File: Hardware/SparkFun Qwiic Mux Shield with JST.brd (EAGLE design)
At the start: 53.3 x 59.7 mm, 35 parts, among them Q1 200mA/50V, Q2 200mA/50V, U1 ARDUINO UNO

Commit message: Adding Mux Shield
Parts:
- removed J21, J22: (no value), SparkX:1X18_NO_SILK
- removed Q1, Q2: 200mA/50V, SparkFun-DiscreteSemi:SOT23-3
- added C1: 0.1uF, SparkFun-Capacitors:0603
- added C2, C3, C4, C5: 1.0uF, SparkFun-Capacitors:0603
- added J23, J24, J25, J26: (no value), SparkX:1X04
- added J29, J30: (no value), SparkFun-Connectors:1X08_NO_SILK
- added JP1, JP2, JP3: (no value), SparkFun-Jumpers:SMT-JUMPER_2_NO_SILK
- added R1, R10, R11, R12, R13, R14, R15, R16, R17, R18, R6, R7, R8, R9: 4.7K, SparkFun-Resistors:0603-RES
- added R19, R20, R21: 10k, SparkFun-Resistors:0603
- added U2: TCA9548A, SparkX:TSSOP28
- J11, J12, J13, J14, J15, J16, J17, J18, J19, J20, J5, J7: device SparkX:1X18_NO_SILK -> SparkFun-Connectors:1X08_NO_SILK
- moved U$1 42.0 mm to (48.3, 6.35)
- moved R4 30.6 mm to (20.3, 17.8)
- moved R5 27.1 mm to (20.3, 20.3)
- moved R3 22.5 mm to (35.6, 25.4), turned to 270 degrees
- moved R2 17.7 mm to (40.6, 25.4), turned to 270 degrees
- moved J11 17.0 mm to (20.3, 39.4), turned to 90 degrees
- moved J17 16.1 mm to (35.6, 39.4), turned to 90 degrees
- moved J19 16.1 mm to (40.6, 39.4), turned to 90 degrees
- moved J5 15.5 mm to (15.2, 39.4), turned to 90 degrees
- moved J13 15.5 mm to (25.4, 39.4), turned to 90 degrees
- moved J15 15.5 mm to (30.5, 39.4), turned to 90 degrees
- moved J12 13.0 mm to (22.9, 57.1)
- moved J16 8.03 mm to (33.0, 57.1)
- moved J14 8.03 mm to (27.9, 57.1)
- moved J18 5.68 mm to (38.1, 57.1)
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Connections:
- removed net HV_SCL: J4.1, Q2.3, R5.2, U1.A5
- removed net HV_SDA: J4.2, Q1.3, R4.2, U1.A4
- removed net N$100: J19.11, J20.11
- removed net N$101: J19.12, J20.12
- removed net N$102: J19.13, J20.13
- removed net N$103: J19.14, J20.14
- removed net N$104: J19.15, J20.15
- removed net N$105: J19.16, J20.16
- removed net N$106: J19.17, J20.17
- removed net N$107: J19.18, J20.18
- removed net N$108: J19.1, J20.1
- removed net N$109: J21.2, J22.2
- removed net N$110: J21.3, J22.3
- removed net N$111: J21.4, J22.4
- removed net N$112: J21.5, J22.5
- removed net N$113: J21.6, J22.6
- removed net N$114: J21.7, J22.7
- removed net N$115: J21.8, J22.8
- removed net N$116: J21.9, J22.9
- removed net N$117: J21.10, J22.10
- removed net N$118: J21.11, J22.11
- removed net N$119: J21.12, J22.12
- removed net N$120: J21.13, J22.13
- removed net N$121: J21.14, J22.14
- removed net N$122: J21.15, J22.15
- removed net N$123: J21.16, J22.16
- removed net N$124: J21.17, J22.17
- removed net N$125: J21.18, J22.18
- removed net N$126: J21.1, J22.1
- removed net N$49: J13.14, J14.14
- removed net N$50: J13.15, J14.15
- removed net N$51: J13.16, J14.16
- removed net N$52: J13.17, J14.17
- removed net N$53: J13.18, J14.18
- removed net N$54: J13.1, J14.1
- removed net N$55: J15.2, J16.2
- removed net N$56: J15.3, J16.3
- removed net N$65: J15.12, J16.12
- removed net N$66: J15.13, J16.13
- removed net N$67: J15.14, J16.14
- removed net N$68: J15.15, J16.15
- removed net N$69: J15.16, J16.16
- removed net N$70: J15.17, J16.17
- removed net N$71: J15.18, J16.18
- removed net N$72: J15.1, J16.1
- removed net N$73: J17.2, J18.2
- removed net N$74: J17.3, J18.3
- removed net N$75: J17.4, J18.4
- removed net N$76: J17.5, J18.5
- removed net N$77: J17.6, J18.6
- removed net N$78: J17.7, J18.7
- removed net N$79: J17.8, J18.8
- removed net N$80: J17.9, J18.9
- removed net N$81: J17.10, J18.10
- removed net N$82: J17.11, J18.11
- removed net N$83: J17.12, J18.12
- removed net N$84: J17.13, J18.13
- removed net N$85: J17.14, J18.14
- removed net N$86: J17.15, J18.15
- removed net N$87: J17.16, J18.16
- removed net N$88: J17.17, J18.17
- removed net N$89: J17.18, J18.18
- removed net N$90: J17.1, J18.1
- removed net N$91: J19.2, J20.2
- removed net N$92: J19.3, J20.3
- removed net N$93: J19.4, J20.4
- removed net N$94: J19.5, J20.5
- removed net N$95: J19.6, J20.6
- removed net N$96: J19.7, J20.7
- removed net N$97: J19.8, J20.8
- removed net N$98: J19.9, J20.9
- removed net N$99: J19.10, J20.10
- removed net SCL: J1.4, J10.4, J8.4, J9.4, Q2.2, R2.2
- removed net SDA: J1.3, J10.3, J8.3, J9.3, Q1.2, R3.2
- new net ADR0: JP3.1, R19.2, U2.1
- new net ADR1: JP2.1, R20.2, U2.2
- new net ADR2: JP1.1, R21.2, U2.21
- new net MAIN_SCL: J4.1, R5.2, U1.A5, U2.22
- new net MAIN_SCL_1: J3.10, U1.SCL
- new net MAIN_SDA: J4.2, R4.2, U1.A4, U2.23
- new net MAIN_SDA_1: J3.9, U1.SDA
- new net SCL0: J1.4, R7.2, U2.5
- new net SCL2: J9.4, R10.2, U2.9
- new net SCL3: J10.4, R12.2, U2.11
- new net SCL4: J23.4, R3.2, U2.14
- new net SCL5: J24.4, R14.2, U2.16
- new net SCL6: J25.4, R16.2, U2.18
- new net SCL7: J26.4, R18.2, U2.20
- new net SDA0: J1.3, R6.2, U2.4
- new net SDA2: J9.3, R9.2, U2.8
- new net SDA3: J10.3, R11.2, U2.10
- new net SDA4: J23.3, R2.2, U2.13
- new net SDA5: J24.3, R13.2, U2.15
- new net SDA6: J25.3, R15.2, U2.17
- new net SDA7: J26.3, R17.2, U2.19
- net 3.3V: now also C1.1, C2.1, C3.1, C4.1, C5.1, J23.2, J24.2, J25.2, J26.2, JP1.2, JP2.2, JP3.2, R1.1, R10.1, R11.1, R12.1, R13.1, R14.1, R15.1, R16.1, R17.1, R18.1, R6.1, R7.1, R8.1, R9.1, U2.24, U2.3; no longer Q1.1, Q2.1
- net GND: now also C1.2, C2.2, C3.2, C4.2, C5.2, J23.1, J24.1, J25.1, J26.1, R19.1, R20.1, R21.1, U2.12
- net N$1: now also J5.8, J7.1; no longer J5.2, J7.2
- net N$10: now also J11.7, J12.2; no longer J5.11, J7.11
- net N$11: now also J11.6, J12.3; no longer J5.12, J7.12
- net N$12: now also J11.5, J12.4; no longer J5.13, J7.13
- net N$13: now also J11.4, J12.5; no longer J5.14, J7.14
- net N$14: now also J11.3, J12.6; no longer J5.15, J7.15
- net N$15: now also J11.2, J12.7; no longer J5.16, J7.16
- net N$16: now also J11.1, J12.8; no longer J5.17, J7.17
- net N$17: now also J13.8, J14.1; no longer J5.18, J7.18
- net N$18: now also J13.7, J14.2; no longer J5.1, J7.1
- net N$19: now also J13.6, J14.3; no longer J13.2, J14.2
- net N$2: now also J5.7, J7.2; no longer J5.3, J7.3
- net N$20: now also J13.5, J14.4; no longer J13.3, J14.3
- net N$21: now also J13.4, J14.5; no longer J11.2, J12.2
- net N$22: now also J13.3, J14.6; no longer J11.3, J12.3
- net N$23: now also J13.2, J14.7; no longer J11.4, J12.4
- net N$24: now also J13.1, J14.8; no longer J11.5, J12.5
- net N$25: now also J15.8, J16.1; no longer J11.6, J12.6
- net N$26: now also J15.7, J16.2; no longer J11.7, J12.7
- net N$27: now also J15.6, J16.3; no longer J11.8, J12.8
- net N$28: now also J15.5, J16.4; no longer J11.9, J12.9
- net N$29: now also J15.4, J16.5; no longer J11.10, J12.10
- net N$3: now also J5.6, J7.3; no longer J5.4, J7.4
- net N$30: now also J15.3, J16.6; no longer J11.11, J12.11
- net N$31: now also J15.2, J16.7; no longer J11.12, J12.12
- net N$32: now also J15.1, J16.8; no longer J11.13, J12.13
- net N$33: now also J17.8, J18.1; no longer J11.14, J12.14
- net N$34: now also J17.7, J18.2; no longer J11.15, J12.15
- net N$35: now also J17.6, J18.3; no longer J11.16, J12.16
- net N$36: now also J17.5, J18.4; no longer J11.17, J12.17
- net N$37: now also J17.4, J18.5; no longer J11.18, J12.18
- net N$38: now also J17.3, J18.6; no longer J11.1, J12.1
- net N$39: now also J17.2, J18.7; no longer J13.4, J14.4
- net N$4: now also J7.4; no longer J7.5
- net N$40: now also J17.1, J18.8; no longer J13.5, J14.5
- net N$41: now also J19.8, J20.1; no longer J13.6, J14.6
- net N$42: now also J19.7, J20.2; no longer J13.7, J14.7
- net N$43: now also J19.6, J20.3; no longer J13.8, J14.8
- net N$44: now also J19.5, J20.4; no longer J13.9, J14.9
- net N$45: now also J19.4, J20.5; no longer J13.10, J14.10
- net N$46: now also J19.3, J20.6; no longer J13.11, J14.11
- net N$47: now also J19.2, J20.7; no longer J13.12, J14.12
- net N$48: now also J19.1, J20.8; no longer J13.13, J14.13
- net N$5: now also J5.4, J7.5; no longer J5.6, J7.6
- net N$57: now also J29.8, J30.1; no longer J15.4, J16.4
- net N$58: now also J29.7, J30.2; no longer J15.5, J16.5
- net N$59: now also J29.6, J30.3; no longer J15.6, J16.6
- net N$6: now also J5.3, J7.6; no longer J5.7, J7.7
- net N$60: now also J29.5, J30.4; no longer J15.7, J16.7
- net N$61: now also J29.4, J30.5; no longer J15.8, J16.8
- net N$62: now also J29.3, J30.6; no longer J15.9, J16.9
- net N$63: now also J29.2, J30.7; no longer J15.10, J16.10
- net N$64: now also J29.1, J30.8; no longer J15.11, J16.11
- net N$7: now also J5.2, J7.7; no longer J5.8, J7.8
- net N$8: now also J5.1, J7.8; no longer J5.9, J7.9
- net N$9: now also J11.8, J12.1; no longer J5.10, J7.10
- net SCL1: now also J8.4, R8.2, U2.7; no longer J3.10, U1.SCL
- net SDA1: now also J8.3, R1.2, U2.6; no longer J3.9, U1.SDA
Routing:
- net 3.3V: track 79.8 -> 200.0 mm
- net MAIN_SDA: track 0.00 -> 69.4 mm, vias 0 -> 1
- net MAIN_SCL: track 0.00 -> 66.9 mm, vias 0 -> 1
- net HV_SCL: track 53.4 -> 0.00 mm, vias 1 -> 0
- net SDA: track 50.0 -> 0.00 mm
- net HV_SDA: track 47.6 -> 0.00 mm
- net SCL: track 45.2 -> 0.00 mm, vias 5 -> 0
- net 5V: track 26.9 -> 52.8 mm, vias 0 -> 1
- net SDA4: track 0.00 -> 20.8 mm
- net SCL0: track 0.00 -> 20.0 mm
- net ADR1: track 0.00 -> 19.1 mm, vias 0 -> 2
- net SCL7: track 0.00 -> 18.7 mm
- net SDA7: track 0.00 -> 18.6 mm
- net SDA0: track 0.00 -> 18.4 mm
- net SDA3: track 0.00 -> 18.0 mm
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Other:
- board text added: "0"
- board text added: "1"
- board text added: "3.3V"
- board text added: "ADR"
- board text added: "Port"
- board text added: "Qwiic Mux Shield"
- board text added: "SCLx"
- board text added: "SDAx"
- board text removed: "I2C Shield"

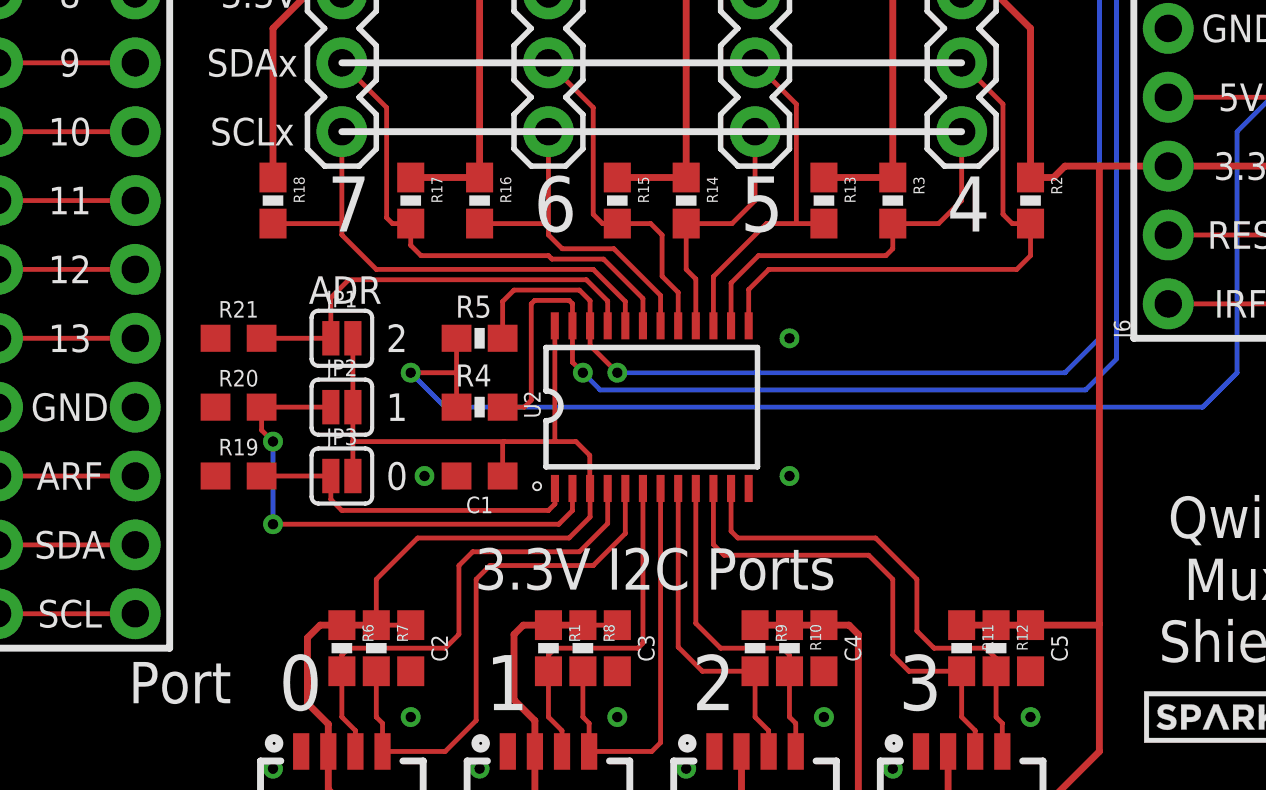
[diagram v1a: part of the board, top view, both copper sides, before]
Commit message: Breaking out reset pin
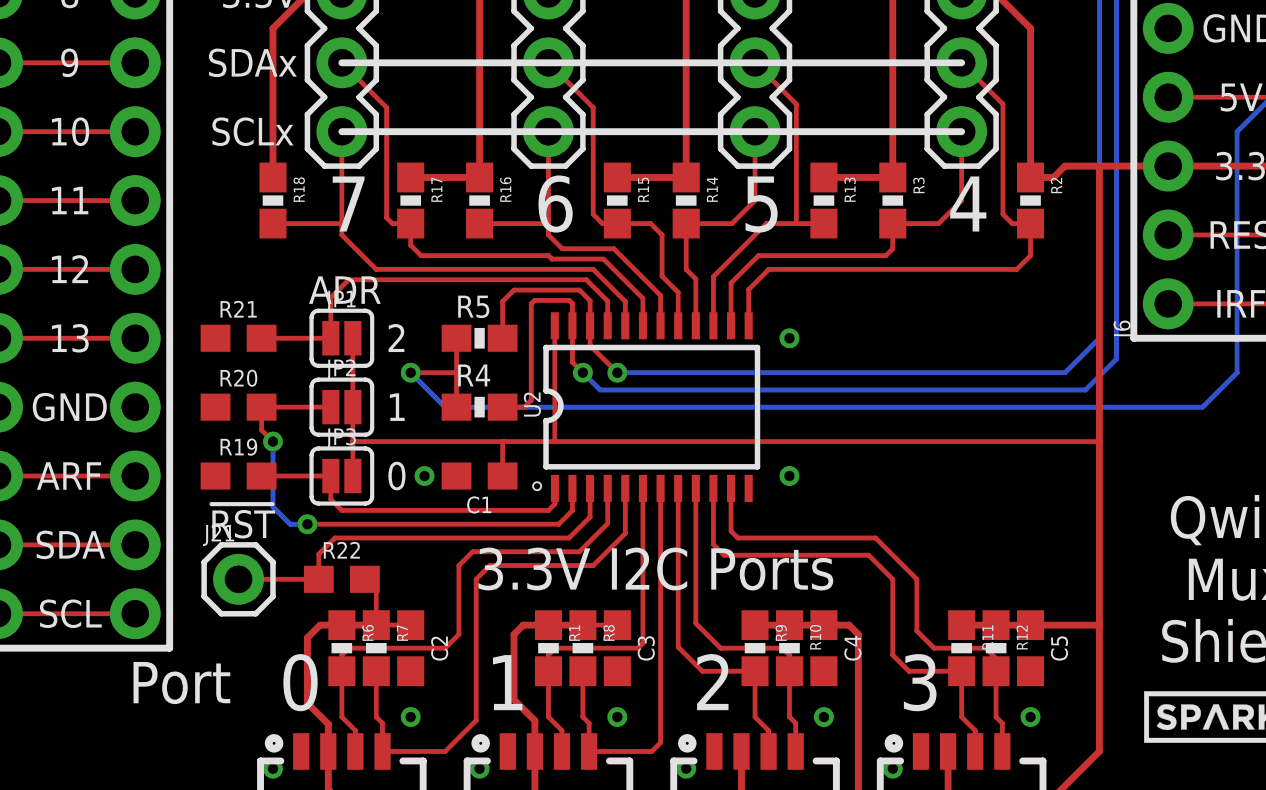
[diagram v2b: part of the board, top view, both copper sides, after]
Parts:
- added J21: (no value), SparkFun-Connectors:1X01
- added R22: 10k, SparkFun-Resistors:0603
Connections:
- new net !RST: J21.1, R22.1, U2.3
- net 3.3V: now also R22.2; no longer U2.3
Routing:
- net !RST: track 0.00 -> 15.5 mm
- net 3.3V: track 200.0 -> 207.4 mm
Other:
- board text added: "!RST"
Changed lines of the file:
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@@
 <layer number="47" name="Measures" color="7" fill="1" visible="no" active="yes"/>
 <layer number="48" name="Document" color="7" fill="1" visible="no" active="yes"/>
-<layer number="49" name="Reference" color="7" fill="1" visible="yes" active="yes"/>
+<layer number="49" name="Reference" color="7" fill="1" visible="no" active="yes"/>
 <layer number="50" name="dxf" color="7" fill="1" visible="no" active="yes"/>
 <layer number="51" name="tDocu" color="6" fill="1" visible="yes" active="yes"/>
@@
 <text x="22.733" y="25.273" size="2.032" layer="22" font="vector" ratio="15" rot="MR0" align="center">6</text>
 <text x="15.113" y="25.273" size="2.032" layer="22" font="vector" ratio="15" rot="MR0" align="center">7</text>
+<text x="11.557" y="13.462" size="1.016" layer="21" font="vector" ratio="15" align="center">!RST</text>
 </plain>
 <attributes>
@@
 <attribute name="PROD_ID" value="CONN-08438" x="43.18" y="57.15" size="1.778" layer="27" rot="R270" display="off"/>
 </element>
+<element name="R22" library="SparkFun-Resistors" package="0603" value="10k" x="15.24" y="11.43">
+<attribute name="PROD_ID" value="RES-00824" x="15.24" y="11.43" size="1.778" layer="27" font="vector" ratio="15" display="off"/>
+</element>
+<element name="J21" library="SparkFun-Connectors" package="1X01" value="" x="11.43" y="11.43"/>
 </elements>
 <signals>
@@
 <contactref element="J10" pad="2"/>
 <contactref element="U2" pad="24"/>
-<contactref element="U2" pad="3"/>
 <contactref element="R6" pad="1"/>
 <contactref element="R7" pad="1"/>
@@
 <wire x1="15.6464" y1="17.78" x2="15.6464" y2="20.32" width="0.1778" layer="1"/>
 <wire x1="21.17" y1="15.24" x2="21.17" y2="16.471" width="0.1778" layer="1"/>
-<wire x1="23.876" y1="16.51" x2="23.114" y2="16.51" width="0.1778" layer="1"/>
-<wire x1="23.114" y1="16.51" x2="21.209" y2="16.51" width="0.1778" layer="1"/>
 <wire x1="21.209" y1="16.51" x2="15.6464" y2="16.51" width="0.1778" layer="1"/>
-<wire x1="23.876" y1="16.51" x2="24.384" y2="16.002" width="0.1778" layer="1"/>
-<wire x1="24.384" y1="16.002" x2="24.384" y2="14.791" width="0.1778" layer="1"/>
-<wire x1="24.384" y1="14.791" x2="24.395" y2="14.78" width="0.1778" layer="1"/>
 <wire x1="21.17" y1="16.471" x2="21.209" y2="16.51" width="0.1778" layer="1"/>
-<wire x1="23.095" y1="20.78" x2="23.095" y2="16.529" width="0.1778" layer="1"/>
-<wire x1="23.095" y1="16.529" x2="23.114" y2="16.51" width="0.1778" layer="1"/>
 <wire x1="14.74" y1="5.08" x2="14.74" y2="3.675" width="0.254" layer="1"/>
 <wire x1="14.74" y1="3.675" x2="14.986" y2="3.429" width="0.254" layer="1"/>
@@
 <wire x1="41.529" y1="3.429" x2="43.18" y2="5.08" width="0.254" layer="1"/>
 <wire x1="43.18" y1="5.08" x2="43.18" y2="9.779" width="0.254" layer="1"/>
-<wire x1="43.18" y1="9.779" x2="43.18" y2="26.67" width="0.254" layer="1"/>
+<wire x1="43.18" y1="9.779" x2="43.18" y2="16.51" width="0.254" layer="1"/>
+<wire x1="43.18" y1="16.51" x2="43.18" y2="26.67" width="0.254" layer="1"/>
 <wire x1="37.6" y1="5.08" x2="37.6" y2="3.437" width="0.254" layer="1"/>
 <wire x1="37.6" y1="3.437" x2="37.592" y2="3.429" width="0.254" layer="1"/>
@@
 <wire x1="15.24" y1="9.74" x2="14.439" y2="9.74" width="0.254" layer="1"/>
 <wire x1="15.24" y1="9.74" x2="16.51" y2="9.74" width="0.254" layer="1"/>
-<wire x1="24.395" y1="14.78" x2="24.395" y2="13.727" width="0.1778" layer="1"/>
-<wire x1="24.395" y1="13.727" x2="23.622" y2="12.954" width="0.1778" layer="1"/>
-<wire x1="23.622" y1="12.954" x2="18.034" y2="12.954" width="0.1778" layer="1"/>
 <contactref element="C2" pad="1"/>
 <contactref element="C3" pad="1"/>
@@
 <wire x1="17.78" y1="9.74" x2="16.51" y2="9.74" width="0.1778" layer="1"/>
 <wire x1="16.51" y1="11.43" x2="16.51" y2="9.74" width="0.1778" layer="1"/>
-<wire x1="18.034" y1="12.954" x2="16.51" y2="11.43" width="0.1778" layer="1"/>
+<contactref element="R22" pad="2"/>
+<wire x1="23.095" y1="20.78" x2="23.095" y2="16.529" width="0.1778" layer="1"/>
+<wire x1="21.209" y1="16.51" x2="23.114" y2="16.51" width="0.1778" layer="1"/>
+<wire x1="23.114" y1="16.51" x2="43.18" y2="16.51" width="0.1778" layer="1"/>
+<wire x1="23.095" y1="16.529" x2="23.114" y2="16.51" width="0.1778" layer="1"/>
+<wire x1="16.51" y1="11.43" x2="16.09" y2="11.43" width="0" layer="19" extent="1-1"/>
 </signal>
 <signal name="MAIN_SDA">
@@
 <wire x1="23.745" y1="14.78" x2="23.745" y2="13.966" width="0.1778" layer="1"/>
 <wire x1="23.745" y1="13.966" x2="23.241" y2="13.462" width="0.1778" layer="1"/>
-<wire x1="23.241" y1="13.462" x2="12.7" y2="13.462" width="0.1778" layer="1"/>
-<via x="12.7" y="13.462" extent="1-16" drill="0.381"/>
-<wire x1="12.7" y1="13.462" x2="12.7" y2="16.51" width="0.1778" layer="16"/>
+<wire x1="23.241" y1="13.462" x2="13.97" y2="13.462" width="0.1778" layer="1"/>
+<via x="13.97" y="13.462" extent="1-16" drill="0.381"/>
 <via x="12.7" y="16.51" extent="1-16" drill="0.381"/>
 <wire x1="12.28" y1="17.78" x2="12.28" y2="16.93" width="0.1778" layer="1"/>
 <wire x1="12.28" y1="16.93" x2="12.7" y2="16.51" width="0.1778" layer="1"/>
+<wire x1="12.7" y1="16.51" x2="12.7" y2="14.097" width="0.1778" layer="16"/>
+<wire x1="12.7" y1="14.097" x2="13.335" y2="13.462" width="0.1778" layer="16"/>
+<wire x1="13.335" y1="13.462" x2="13.97" y2="13.462" width="0.1778" layer="16"/>
 </signal>
 <signal name="ADR0">
@@
 <wire x1="40.64" y1="39.37" x2="43.18" y2="39.37" width="0.1778" layer="1"/>
 </signal>
+<signal name="!RST">
+<contactref element="U2" pad="3"/>
+<contactref element="R22" pad="1"/>
+<contactref element="J21" pad="1"/>
+<wire x1="24.395" y1="14.78" x2="24.395" y2="13.727" width="0.1778" layer="1"/>
+<wire x1="24.395" y1="13.727" x2="23.622" y2="12.954" width="0.1778" layer="1"/>
+<wire x1="23.622" y1="12.954" x2="14.986" y2="12.954" width="0.1778" layer="1"/>
+<wire x1="14.986" y1="12.954" x2="14.39" y2="12.358" width="0.1778" layer="1"/>
+<wire x1="14.39" y1="11.43" x2="14.39" y2="12.358" width="0.1778" layer="1"/>
+<wire x1="14.39" y1="11.43" x2="11.43" y2="11.43" width="0.1778" layer="1"/>
+</signal>
 </signals>
